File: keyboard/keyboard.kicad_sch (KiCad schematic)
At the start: 145 parts, among them J1 col, J10 col, J11 col, J12 col, J13 col, J14 col, J15 row, J16 row, J17 row, J18 row, J19 row, J2 col, J3 col, J4 col, J5 col, J6 col, J7 col, J8 col, J9 col

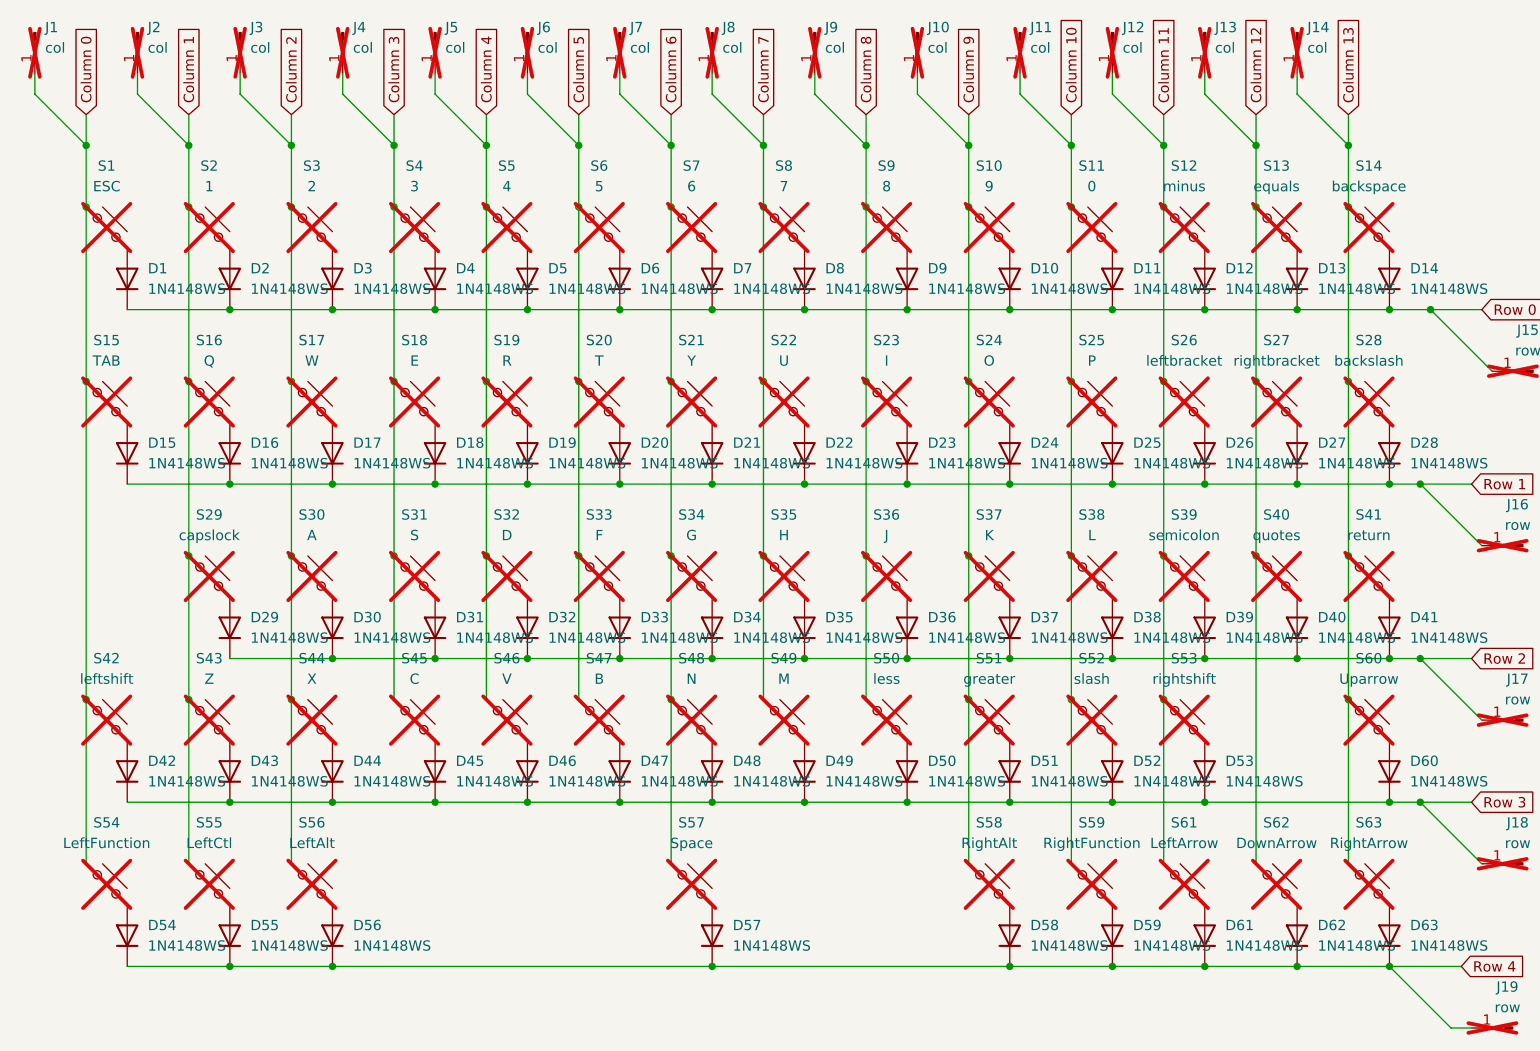
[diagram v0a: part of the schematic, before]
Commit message: Updated with reference switches
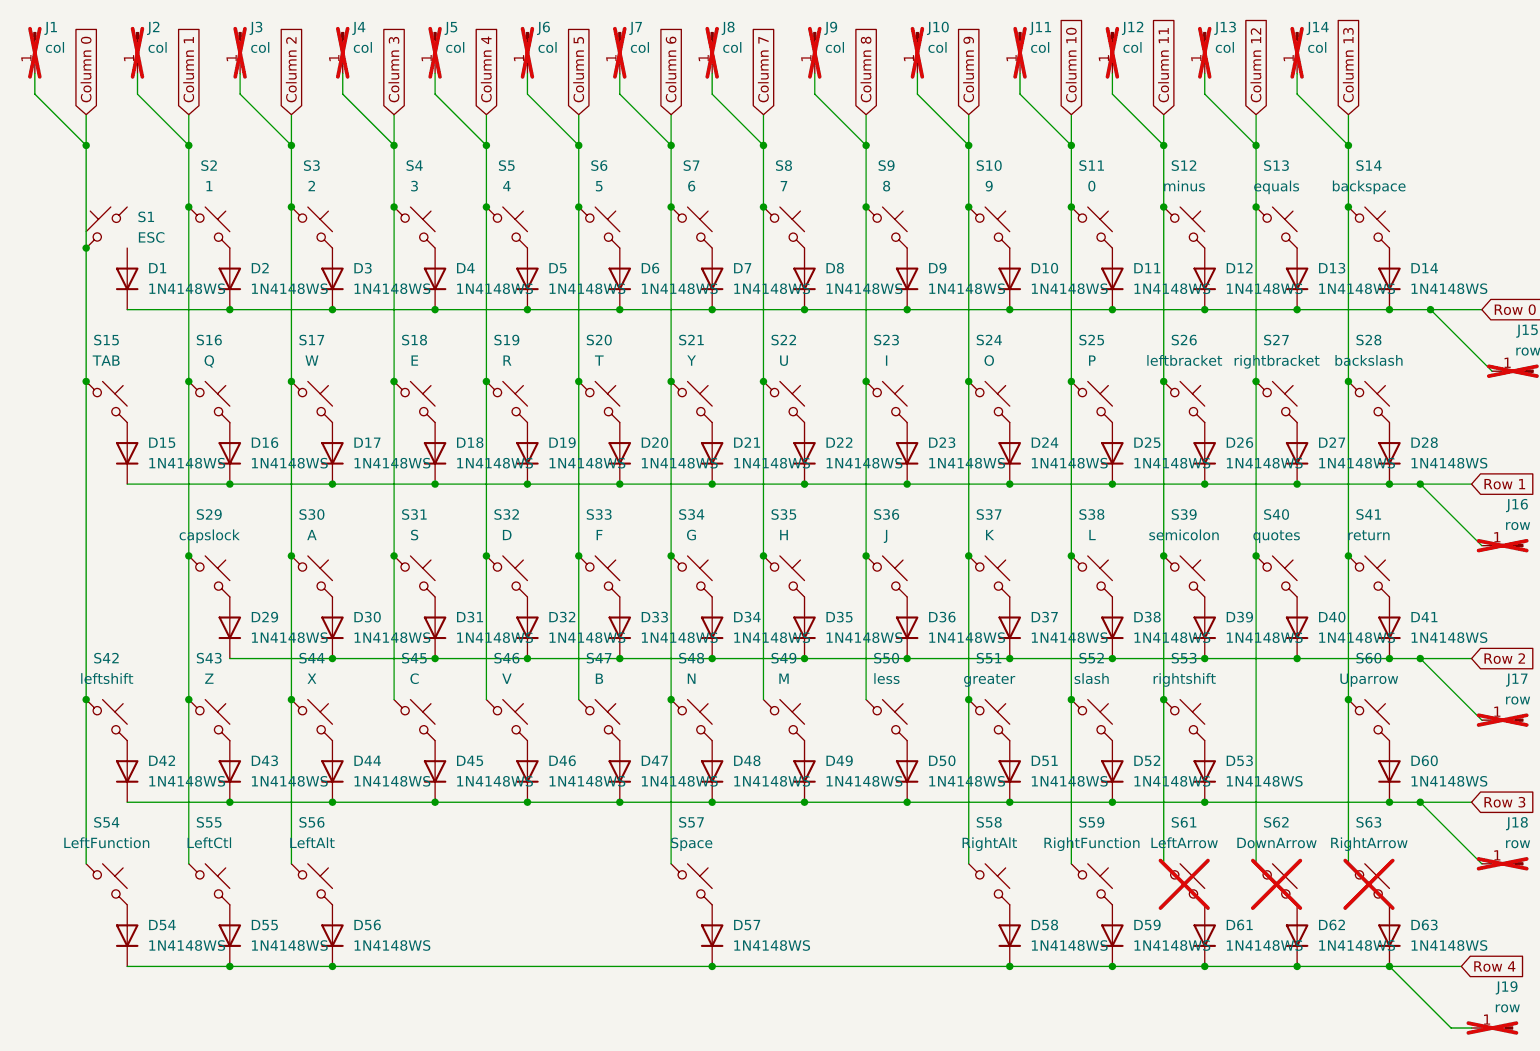
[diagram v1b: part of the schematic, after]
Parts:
- S1, S10, S11, S12, S13, S16, S17, S18, S19, S2, S20, S21, S22, S23, S24, S25, S26, S27, S3, S30, S31, S32, S33, S34, S35, S36, S37, S38, S39, S4, S40, S43, S44, S45, S46, S47, S48, S49, S5, S50, S51, S52, S55, S59, S6, S60, S7, S8, S9: footprint Button_Switch_Keyboard:SW_Cherry_MX_1.00u_PCB -> sandpiperfootprints:SW_Cherry_MX_1.00u_PCB; now fitted
- S14, S15, S28, S29, S41, S42, S53, S54, S56, S57, S58: now fitted
- S61, S62, S63: footprint Button_Switch_Keyboard:SW_Cherry_MX_1.00u_PCB -> sandpiperfootprints:SW_Cherry_MX_1.00u_PCB
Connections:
- net at S1.2: no longer D1.2 (A)

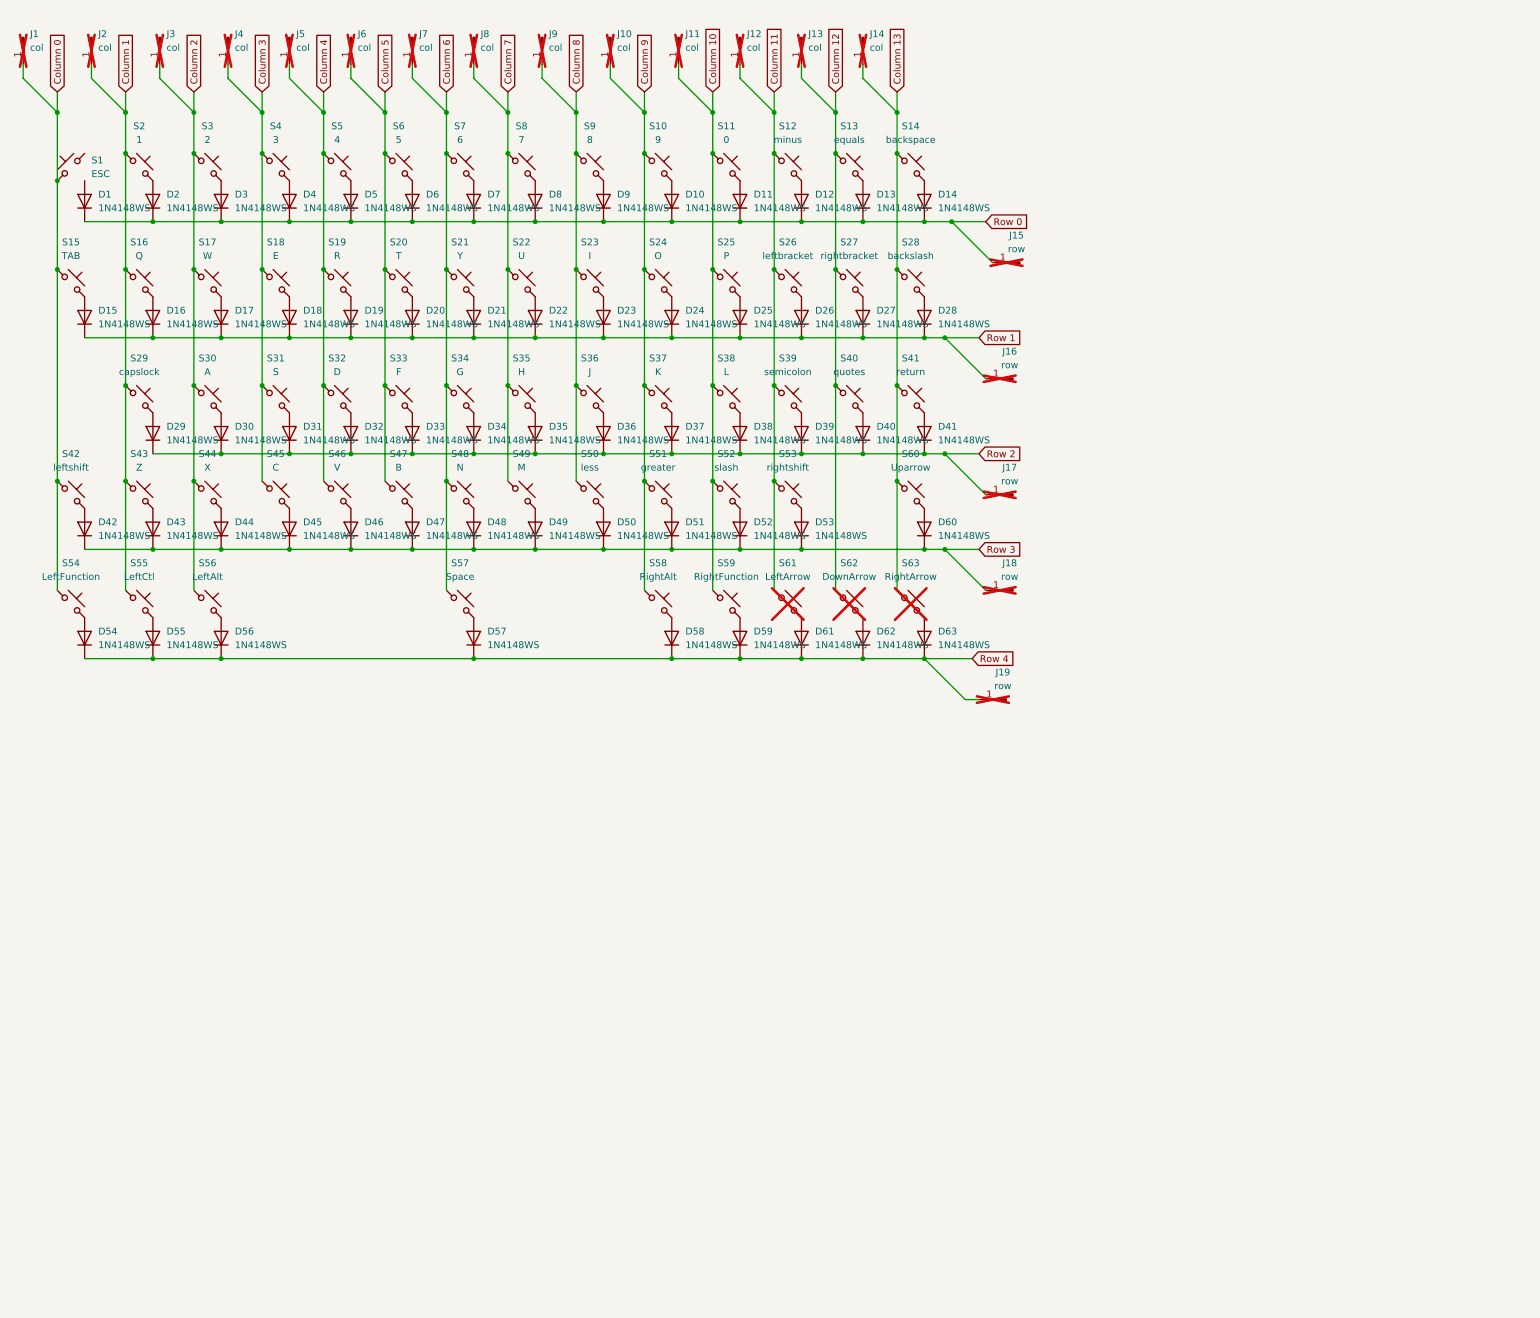
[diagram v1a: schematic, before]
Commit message: USB keyboard instead
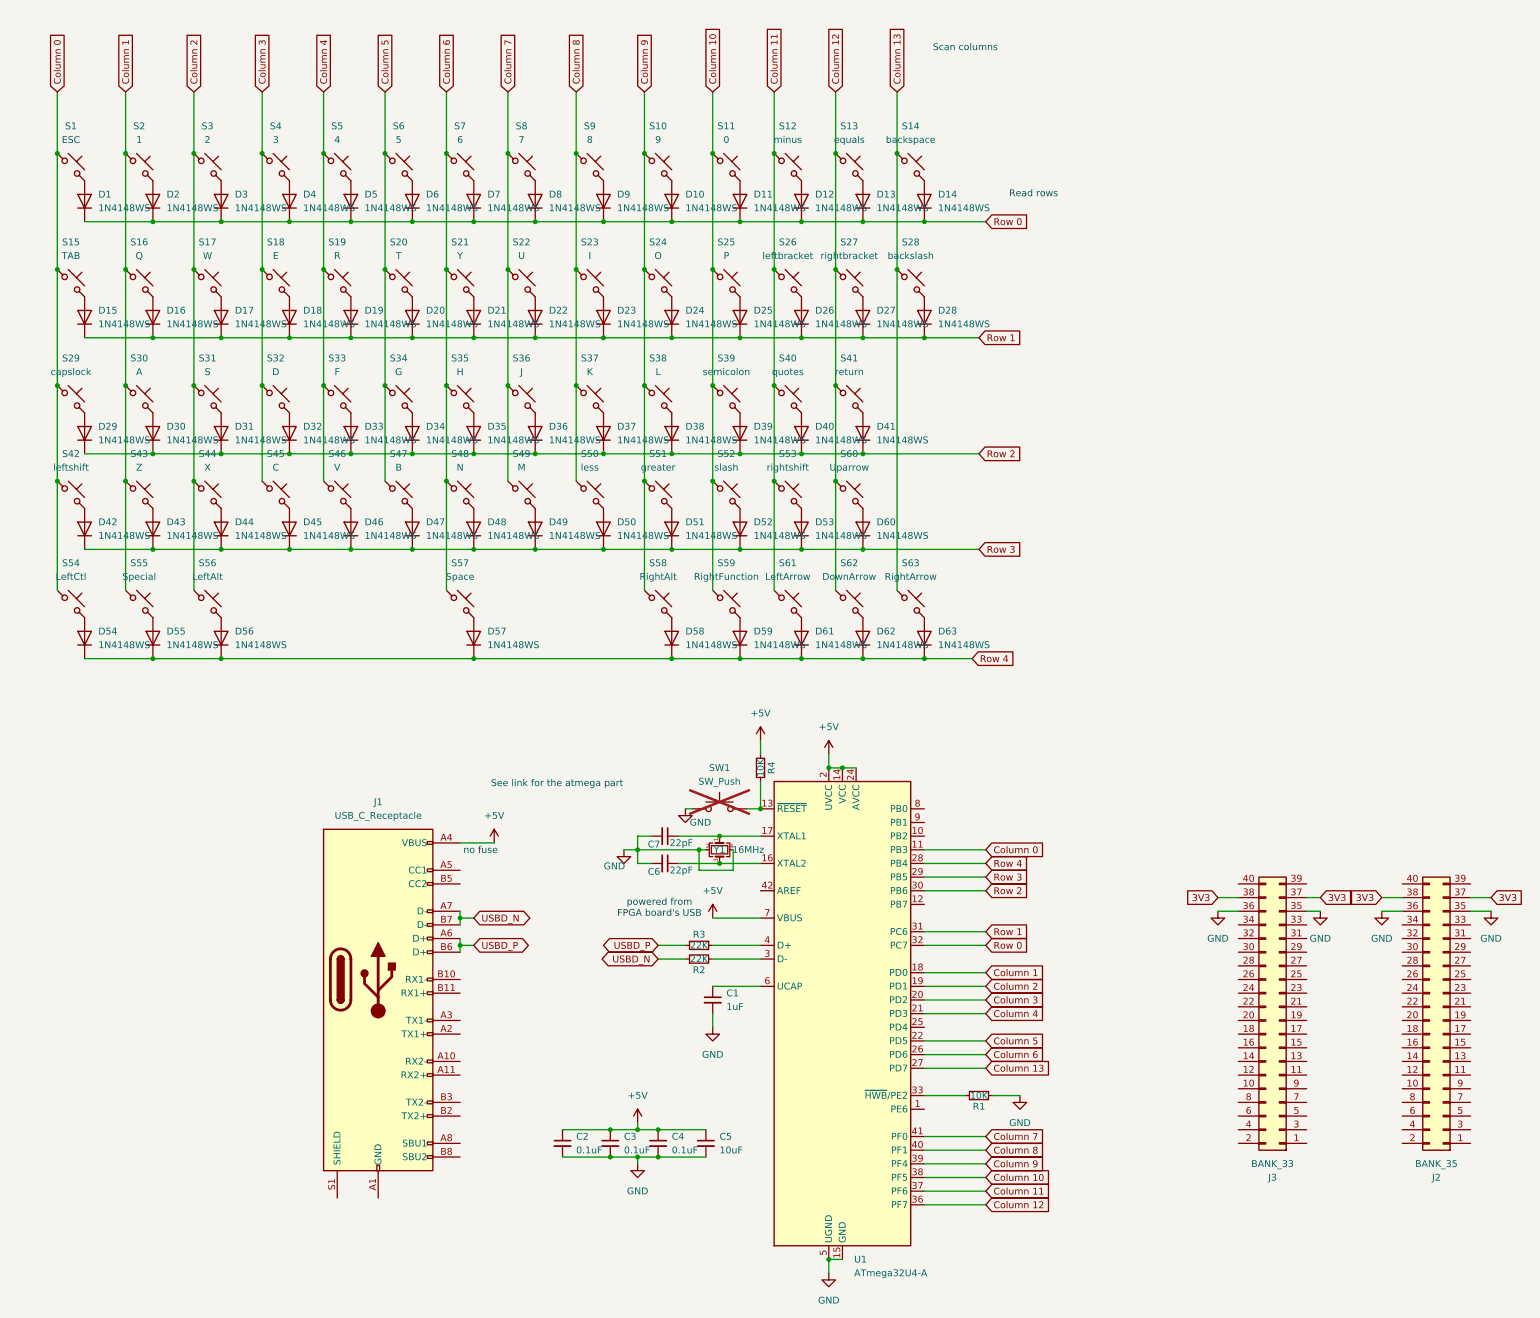
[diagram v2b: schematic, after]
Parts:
- removed J1, J10, J11, J12, J13, J14, J2, J3, J4, J5, J6, J7, J8, J9: col, TestPoint:TestPoint_THTPad_2.0x2.0mm_Drill1.0mm, symbol Connector:Conn_01x01_Pin
- removed J15, J16, J17, J18, J19: row, TestPoint:TestPoint_THTPad_2.0x2.0mm_Drill1.0mm, symbol Connector:Conn_01x01_Pin
- added C1: 1uF, Capacitor_SMD:C_0805_2012Metric, symbol Device:C_Small
- added C2, C3, C4: 0.1uF, Capacitor_SMD:C_0805_2012Metric, symbol Device:C_Small
- added C5: 10uF, Capacitor_SMD:C_0805_2012Metric, symbol Device:C_Small
- added C6, C7: 22pF, Capacitor_SMD:C_0805_2012Metric, symbol Device:C_Small
- added J1: USB_C_Receptacle, Connector_USB:USB_C_Receptacle_GCT_USB4085, symbol Connector:USB_C_Receptacle
- added J2: BANK_35, Connector_PinHeader_2.54mm:PinHeader_2x20_P2.54mm_Vertical, symbol Connector_Generic:Conn_02x20_Odd_Even
- added J3: BANK_33, Connector_PinHeader_2.54mm:PinHeader_2x20_P2.54mm_Vertical, symbol Connector_Generic:Conn_02x20_Odd_Even
- added R1, R4: 10K, Resistor_SMD:R_0805_2012Metric, symbol Device:R_Small
- added R2, R3: 22K, Resistor_SMD:R_0805_2012Metric, symbol Device:R_Small
- added SW1: SW_Push, Button_Switch_SMD:SW_Tactile_SPST_NO_Straight_CK_PTS636Sx25SMTRLFS, symbol Switch:SW_Push
- added U1: ATmega32U4-A, Package_QFP:TQFP-44_10x10mm_P0.8mm, symbol MCU_Microchip_ATmega:ATmega32U4-A
- added Y1: 16MHz, Crystal:Crystal_SMD_3225-4Pin_3.2x2.5mm, symbol Device:Crystal_GND24_Small
- S14: footprint Button_Switch_Keyboard:SW_Cherry_MX_2.00u_PCB -> sandpiperfootprints:SW_Cherry_MX_1.00u_PCB
- S15, S28: footprint Button_Switch_Keyboard:SW_Cherry_MX_1.50u_PCB -> sandpiperfootprints:SW_Cherry_MX_1.00u_PCB
- S29: footprint Button_Switch_Keyboard:SW_Cherry_MX_1.75u_PCB -> sandpiperfootprints:SW_Cherry_MX_1.00u_PCB
- S54: value LeftFunction -> LeftCtl
- S55: value LeftCtl -> Special
- S61, S62, S63: now fitted
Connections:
- net Column 0: now also S29.1, U1.11 (PB3)
- net Column 1: now also S30.1, U1.18 (PD0); no longer S29.1
- net Column 10: now also S39.1, U1.38 (PF5); no longer S38.1
- net Column 11: now also S40.1, U1.37 (PF6); no longer S39.1
- net Column 12: now also S41.1, S60.1, U1.36 (PF7); no longer S40.1
- net Column 13: now also U1.27 (PD7); no longer S41.1, S60.1
- net Column 2: now also S31.1, U1.19 (PD1); no longer S30.1
- net Column 3: now also S32.1, U1.20 (PD2); no longer S31.1
- net Column 4: now also S33.1, U1.21 (PD3); no longer S32.1
- net Column 5: now also S34.1, U1.22 (PD5); no longer S33.1
- net Column 6: now also S35.1, U1.26 (PD6); no longer S34.1
- net Column 7: now also S36.1, U1.41 (PF0); no longer S35.1
- net Column 8: now also S37.1, U1.40 (PF1); no longer S36.1
- net Column 9: now also S38.1, U1.39 (PF4); no longer S37.1
- net Row 0: now also U1.32 (PC7)
- net Row 1: now also U1.31 (PC6)
- net Row 2: now also U1.30 (PB6)
- net Row 3: now also U1.29 (PB5)
- net Row 4: now also U1.28 (PB4)
- net at S1.2: now also D1.2 (A)
- new net: J1.A1 (GND), J1.A12 (GND), J1.B1 (GND), J1.B12 (GND)
- new net: C1.1, U1.6 (UCAP)
- new net: C7.1, U1.17 (XTAL1), Y1.1
- new net: C6.1, U1.16 (XTAL2), Y1.3
- new net: R4.1, SW1.2, U1.13 (~{RESET})
- new net: R3.1, U1.4 (D+)
- new net: R2.2, U1.3 (D-)
- new net: R1.1, U1.33 (~{HWB}/PE2)
- new net +5V: C2.1, C3.1, C4.1, C5.1, J1.A4 (VBUS), J1.A9 (VBUS), J1.B4 (VBUS), J1.B9 (VBUS), R4.2, U1.14 (VCC), U1.2 (UVCC), U1.24 (AVCC), U1.34 (VCC), U1.44 (AVCC), U1.7 (VBUS)
- new net 3V3: J2.37 (Pin_37), J2.38 (Pin_38), J3.37 (Pin_37), J3.38 (Pin_38)
- new net GND: C1.2, C2.2, C3.2, C4.2, C5.2, C6.2, C7.2, J2.35 (Pin_35), J2.36 (Pin_36), J3.35 (Pin_35), J3.36 (Pin_36), R1.2, SW1.1, U1.15 (GND), U1.23 (GND), U1.35 (GND), U1.43 (GND), U1.5 (UGND), Y1.2, Y1.4
- new net USBD_N: J1.A7 (D-), J1.B7 (D-), R2.1
- new net USBD_P: J1.A6 (D+), J1.B6 (D+), R3.2
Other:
- note added: "Read rows"
- note added: "Scan columns"
- note added: "See link for the atmega part"
- note added: "no fuse"
- note added: "powered from FPGA board's USB"
- moved on the sheet: D29, D30, D31, D32, D33, D34, D35, D36, D37, D38, D39, D40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
